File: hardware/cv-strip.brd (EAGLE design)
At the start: 152.5 x 43.6 mm, 83 parts, among them IC1 PIC16F1825SO14, IC2 74HC595D, IC3 74HC595D, IC4 MCP4728_QUAD_DAC, IC5 LM324D, IC6 REG1117, IC7 6N138

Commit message: add comp values
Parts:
- C18, C19, C9: value (none) -> 100n
- R17, R18, R19, R20, R23, R24, R25, R26: value (none) -> 100k
- R21, R22: value (none) -> 4k7
- R27, R28: value (none) -> 1k5
- R4: value (none) -> 10k
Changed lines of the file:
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@@
 <attribute name="VALUE" x="55.118" y="12.319" size="1.27" layer="28" rot="MR90"/>
 </element>
-<element name="R22" library="rcl" package="R0805" value="" x="63.5" y="33.02" smashed="yes" rot="MR270">
+<element name="R22" library="rcl" package="R0805" value="4k7" x="63.5" y="33.02" smashed="yes" rot="MR270">
 <attribute name="NAME" x="61.214" y="30.988" size="1.27" layer="26" rot="MR90"/>
-<attribute name="VALUE" x="66.04" y="33.655" size="1.27" layer="28" rot="MR270"/>
-</element>
-<element name="R21" library="rcl" package="R0805" value="" x="66.04" y="33.02" smashed="yes" rot="MR270">
+</element>
+<element name="R21" library="rcl" package="R0805" value="4k7" x="66.04" y="33.02" smashed="yes" rot="MR270">
 <attribute name="NAME" x="68.58" y="34.417" size="1.27" layer="26" rot="MR270"/>
-<attribute name="VALUE" x="68.58" y="33.655" size="1.27" layer="28" rot="MR270"/>
 </element>
 <element name="IC5" library="linear" package="SO14" value="LM324D" x="50.165" y="36.83" smashed="yes" rot="MR270">
 <attribute name="NAME" x="53.848" y="35.306" size="1.27" layer="26" rot="MR90"/>
 </element>
-<element name="R17" library="rcl" package="R0805" value="" x="57.15" y="40.64" smashed="yes" rot="MR0">
+<element name="R17" library="rcl" package="R0805" value="100k" x="57.15" y="40.64" smashed="yes" rot="MR0">
 <attribute name="NAME" x="62.611" y="40.132" size="1.27" layer="26" rot="MR0"/>
-<attribute name="VALUE" x="57.785" y="38.1" size="1.27" layer="28" rot="MR0"/>
-</element>
-<element name="R20" library="rcl" package="R0805" value="" x="57.023" y="33.02" smashed="yes" rot="MR0">
+</element>
+<element name="R20" library="rcl" package="R0805" value="100k" x="57.023" y="33.02" smashed="yes" rot="MR0">
 <attribute name="NAME" x="60.325" y="30.607" size="1.27" layer="26" rot="MR0"/>
-<attribute name="VALUE" x="57.658" y="30.48" size="1.27" layer="28" rot="MR0"/>
-</element>
-<element name="R26" library="rcl" package="R0805" value="" x="43.18" y="33.02" smashed="yes" rot="MR180">
+</element>
+<element name="R26" library="rcl" package="R0805" value="100k" x="43.18" y="33.02" smashed="yes" rot="MR180">
 <attribute name="NAME" x="37.846" y="33.655" size="1.27" layer="26" rot="MR180"/>
-<attribute name="VALUE" x="42.545" y="35.56" size="1.27" layer="28" rot="MR180"/>
-</element>
-<element name="R23" library="rcl" package="R0805" value="" x="43.18" y="40.64" smashed="yes" rot="MR180">
+</element>
+<element name="R23" library="rcl" package="R0805" value="100k" x="43.18" y="40.64" smashed="yes" rot="MR180">
 <attribute name="NAME" x="37.846" y="38.735" size="1.27" layer="26" rot="MR180"/>
-<attribute name="VALUE" x="42.545" y="43.18" size="1.27" layer="28" rot="MR180"/>
-</element>
-<element name="R18" library="rcl" package="R0805" value="" x="57.15" y="38.354" smashed="yes" rot="MR0">
+</element>
+<element name="R18" library="rcl" package="R0805" value="100k" x="57.15" y="38.354" smashed="yes" rot="MR0">
 <attribute name="NAME" x="62.611" y="38.227" size="1.27" layer="26" rot="MR0"/>
-<attribute name="VALUE" x="57.785" y="35.814" size="1.27" layer="28" rot="MR0"/>
-</element>
-<element name="R19" library="rcl" package="R0805" value="" x="57.023" y="35.306" smashed="yes" rot="MR0">
+</element>
+<element name="R19" library="rcl" package="R0805" value="100k" x="57.023" y="35.306" smashed="yes" rot="MR0">
 <attribute name="NAME" x="62.357" y="34.417" size="1.27" layer="26" rot="MR0"/>
-<attribute name="VALUE" x="57.658" y="32.766" size="1.27" layer="28" rot="MR0"/>
-</element>
-<element name="R25" library="rcl" package="R0805" value="" x="43.18" y="35.56" smashed="yes" rot="MR0">
+</element>
+<element name="R25" library="rcl" package="R0805" value="100k" x="43.18" y="35.56" smashed="yes" rot="MR0">
 <attribute name="NAME" x="41.148" y="34.925" size="1.27" layer="26" rot="MR0"/>
-<attribute name="VALUE" x="43.815" y="33.02" size="1.27" layer="28" rot="MR0"/>
-</element>
-<element name="R24" library="rcl" package="R0805" value="" x="43.18" y="38.1" smashed="yes" rot="MR0">
+</element>
+<element name="R24" library="rcl" package="R0805" value="100k" x="43.18" y="38.1" smashed="yes" rot="MR0">
 <attribute name="NAME" x="41.021" y="40.005" size="1.27" layer="26" rot="MR0"/>
-<attribute name="VALUE" x="43.815" y="35.56" size="1.27" layer="28" rot="MR0"/>
 </element>
 <element name="C13" library="rcl" package="C0805" value="" x="89.662" y="1.143" smashed="yes" rot="MR180">
@@
 <attribute name="VALUE" x="88.392" y="3.683" size="1.27" layer="28" rot="MR180"/>
 </element>
-<element name="C9" library="rcl" package="C0805" value="" x="87.122" y="29.718" smashed="yes" rot="MR0">
+<element name="C9" library="rcl" package="C0805" value="100n" x="87.122" y="29.718" smashed="yes" rot="MR0">
 <attribute name="NAME" x="88.773" y="27.178" size="1.27" layer="26" rot="MR0"/>
-<attribute name="VALUE" x="88.392" y="27.178" size="1.27" layer="28" rot="MR0"/>
-</element>
-<element name="C19" library="rcl" package="C0805" value="" x="57.023" y="29.464" smashed="yes" rot="MR0">
+</element>
+<element name="C19" library="rcl" package="C0805" value="100n" x="57.023" y="29.464" smashed="yes" rot="MR0">
 <attribute name="NAME" x="56.388" y="27.051" size="1.27" layer="26" rot="MR0"/>
-<attribute name="VALUE" x="58.293" y="26.924" size="1.27" layer="28" rot="MR0"/>
 </element>
 <element name="C17" library="rcl" package="C0805" value="" x="66.675" y="13.081" smashed="yes" rot="MR270">
@@
 <attribute name="NAME" x="22.903" y="32.0118" size="1" layer="22" rot="MR270"/>
 </element>
-<element name="R27" library="rcl" package="R0805" value="" x="31.75" y="36.83" smashed="yes" rot="MR90">
+<element name="R27" library="rcl" package="R0805" value="1k5" x="31.75" y="36.83" smashed="yes" rot="MR90">
 <attribute name="NAME" x="29.083" y="35.306" size="1.27" layer="26" rot="MR90"/>
-<attribute name="VALUE" x="29.21" y="36.195" size="1.27" layer="28" rot="MR90"/>
-</element>
-<element name="R28" library="rcl" package="R0805" value="" x="30.48" y="31.75" smashed="yes" rot="MR270">
+</element>
+<element name="R28" library="rcl" package="R0805" value="1k5" x="30.48" y="31.75" smashed="yes" rot="MR270">
 <attribute name="NAME" x="33.147" y="32.004" size="1.27" layer="26" rot="MR270"/>
-<attribute name="VALUE" x="33.02" y="32.385" size="1.27" layer="28" rot="MR270"/>
 </element>
 <element name="DRM1" library="jason_eagle6" package="VERTICAL_3_5MM_SOCKET" value="VERTICAL_3_5MM_SOCKET" x="106.68" y="21.59" smashed="yes">
@@
 <attribute name="VALUE" x="110.998" y="40.64" size="1.27" layer="27" ratio="10" rot="R180"/>
 </element>
-<element name="R4" library="rcl" package="R0805" value="" x="100.33" y="35.56" smashed="yes" rot="MR270">
+<element name="R4" library="rcl" package="R0805" value="10k" x="100.33" y="35.56" smashed="yes" rot="MR270">
 <attribute name="NAME" x="101.6" y="36.068" size="1.27" layer="26" rot="MR180"/>
-<attribute name="VALUE" x="102.87" y="36.195" size="1.27" layer="28" rot="MR270"/>
-</element>
-<element name="C18" library="rcl" package="C0805" value="" x="62.23" y="36.83" smashed="yes" rot="MR180">
+</element>
+<element name="C18" library="rcl" package="C0805" value="100n" x="62.23" y="36.83" smashed="yes" rot="MR180">
 <attribute name="NAME" x="64.643" y="37.465" size="1.27" layer="26" rot="MR180"/>
-<attribute name="VALUE" x="60.96" y="39.37" size="1.27" layer="28" rot="MR180"/>
 </element>
 <element name="U$2" library="jason_eagle6" package="PWR_SOCKET_2_1MM" value="PWR_SOCKET_2_1MM" x="138.905" y="35.687" smashed="yes" rot="R45"/>

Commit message: rev2 updates - checking needed
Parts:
- removed CLK1, CLK2, DRM1, DRM2, DRM3, DRM4, DRM5, DRM6, DRM7, DRM8, GATE1, GATE2, NOTE1CV, NOTE2CV, VEL1CV, VEL2CV: VERTICAL_3_5MM_SOCKET, jason_eagle6:VERTICAL_3_5MM_SOCKET
- removed D2: 1N4004, jasons_stuff:DO-VERT
- removed L1, L2, L3: (no value), led:LED3MM
- removed S1: (no value), switch-omron:B3F-10XX
- added ACT, PWR, STA: (no value), led:LED3MM
- added C22: (no value), microbuilder:EIA3216-18/A-R
- added CVA, CVB, CVC, CVD, GT1, GT10, GT11, GT12, GT2, GT3, GT4, GT5, GT6, GT7, GT8, GT9: VERTICAL_3_5MM_SOCKET, jason_eagle6:VERTICAL_3_5MM_SOCKET
- added D3, D4, D5: (no value), microbuilder:SOD-123
- added MODE: (no value), switch-omron:B3F-10XX
- added Q1, Q2, Q4: (no value), microbuilder:SOT363
- added Q3, Q5: (no value), microbuilder:SOT23-R
- added R30, R31, R32, R33, R34, R35, R36, R37, R38, R39: (no value), rcl:R0805
- IC2: value 74HC595D -> AD5696R; device 74xx-eu:SO16 -> jason_eagle6:SSOP16
- IC3: value 74HC595D -> MC14094B; device 74xx-eu:SO16 -> jason_eagle6:SO16
- IC4: value MCP4728_QUAD_DAC -> MC14094B; device jason_eagle6:MSOP10 -> jason_eagle6:SO16
- moved IC4 55.4 mm to (100.6, 7.49)
- moved IC2 47.1 mm to (57.1, 32.3)
- moved R8 15.3 mm to (108.0, 11.4), turned to 180 degrees
- moved R10 14.0 mm to (128.9, 26.9), turned to 270 degrees
- moved R12 13.9 mm to (103.6, 26.7)
- moved R11 13.8 mm to (116.2, 26.5), turned to 270 degrees
- moved C7 11.7 mm to (120.7, 24.1), turned to 180 degrees
- moved C8 11.7 mm to (108.0, 24.1), turned to 180 degrees
- moved C6 11.6 mm to (133.3, 24.1), turned to 180 degrees
- moved R6 11.6 mm to (129.4, 14.2)
- moved R7 11.5 mm to (116.2, 14.2)
- moved C13 11.4 mm to (83.8, 10.9), turned to 270 degrees
- moved C4 9.72 mm to (112.3, 16.0), turned to 90 degrees
- moved C3 9.59 mm to (125.0, 16.1), turned to 90 degrees
- moved C2 9.55 mm to (137.2, 16.1), turned to 90 degrees
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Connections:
- removed net MIDI_OUT: IC1.6
- removed net N$22: IC1.9, IC4.3, R21.2
- removed net N$47: IC2.3, R5.1
- removed net N$51: IC2.4, R12.1
- removed net N$53: IC2.7, R9.1
- new net GT1_VSEL: IC1.6, R38.1
- new net GT2_VSEL: IC1.7, R39.1
- new net N$10: IC3.5, R15.1
- new net N$11: IC3.7, R16.1
- new net N$14: IC3.1, Q1.3, R31.1
- new net N$17: IC4.11, R9.1
- new net N$18: IC4.12, R10.1
- new net N$19: IC4.13, R11.1
- new net N$38: IC4.14, R12.1
- new net N$44: IC4.6, R6.1
- new net N$45: IC4.5, R7.1
- new net SCL: IC1.10, IC2.P$13, R22.2
- new net SDA: IC1.9, IC2.P$8, R21.2
- new net VDD_GT1: C13.1, D3.C, IC3.15, IC3.16, Q3.3, R30.2, R31.2, R32.2
- new net VDD_GT2: C12.1, D4.C, IC4.15, IC4.16, Q5.3, R33.2, R34.2, R35.2
- net ACT_LED: now also ACT.A; no longer L1.A
- net GND: now also C22.-, C9.2, CVA.2, CVB.2, CVC.2, CVD.2, GT1.2, GT10.2, GT11.2, GT12.2, GT2.2, GT3.2, GT4.2, GT5.2, GT6.2, GT7.2, GT8.2, GT9.2, IC2.P$12, IC2.P$14, IC2.P$16, IC2.P$4, IC2.P$9, IC4.8, MODE.3, MODE.4, Q1.1, Q1.4, Q2.1, Q2.4, Q4.1, Q4.4; no longer C9.1, CLK1.2, CLK2.2, DRM1.2, DRM2.2, DRM3.2, DRM4.2, DRM5.2, DRM6.2, DRM7.2, DRM8.2, GATE1.2, GATE2.2, IC2.13, IC2.8, IC3.13, IC4.10, IC4.4, NOTE1CV.2, NOTE2CV.2, S1.3, S1.4, VEL1CV.2, VEL2CV.2
- net N$1: now also GT4.4; no longer CLK2.4
- net N$12: now also IC3.6, R14.1; no longer IC3.15, R15.1
- net N$13: now also IC3.4, R13.1; no longer IC3.1, R16.1
- net N$15: now also IC3.2, Q1.6, R30.1; no longer IC3.3, R13.1
- net N$16: now also IC3.3, Q2.6, R32.1; no longer IC3.2, R14.1
- net N$2: now also CVD.4; no longer VEL2CV.4
- net N$20: now also GT9.4; no longer DRM1.4
- net N$21: now also Q5.1, R37.1, R39.2; no longer IC1.10, IC4.2, R22.2
- net N$23: now also GT10.4; no longer DRM2.4
- net N$24: now also GT11.4; no longer DRM3.4
- net N$3: now also CVB.4; no longer VEL1CV.4
- net N$32: now also GT8.4; no longer DRM4.4
- net N$33: now also GT5.4; no longer DRM5.4
- net N$34: now also MODE.1, MODE.2, R4.2
- net N$35: now also PWR.K; no longer L3.K
- net N$36: now also ACT.K; no longer L1.K
- net N$37: now also STA.K; no longer L2.K
- net N$39: now also GT6.4; no longer DRM6.4
- net N$4: now also CVC.4; no longer NOTE1CV.4
- net N$40: now also D5.A; no longer D2.A
- net N$41: now also GT7.4; no longer DRM7.4
- net N$43: now also IC4.7, R5.1; no longer IC2.15, R8.1
- net N$46: now also IC4.4, R8.1; no longer IC2.1, R7.1
- net N$48: now also IC4.1, Q2.3, R33.1; no longer IC2.2, R6.1
- net N$49: now also IC4.2, Q4.3, R34.1; no longer IC2.5, R11.1
- net N$5: now also CVA.4; no longer NOTE2CV.4
- net N$50: now also IC4.3, Q4.6, R35.1; no longer IC2.6, R10.1
- net N$52: now also GT12.4; no longer DRM8.4
- net N$6: now also GT3.4; no longer GATE2.4
- net N$7: now also GT1.4; no longer GATE1.4
- net N$8: now also GT2.4; no longer CLK1.4
- net N$9: now also Q3.1, R36.1, R38.2; no longer IC1.7, R4.2, S1.1, S1.2
- net SR_CLK: now also Q2.5, Q4.5; no longer IC2.11, IC3.11
- net SR_DAT: now also Q1.5; no longer IC3.14
- net SR_DAT2: now also Q4.2; no longer IC2.14
- net SR_RCK: now also Q1.2, Q2.2; no longer IC2.12, IC3.12
- net STATUS_LED: now also STA.A; no longer L2.A
- net VDD: now also C22.+, C9.1, D3.A, D4.A, IC2.P$10, IC2.P$11, IC2.P$15, IC2.P$5, PWR.A; no longer C12.1, C13.1, C9.2, IC2.10, IC2.16, IC3.10, IC3.16, IC4.1, L3.A
- net VIN: now also D5.C, Q3.2, Q5.2, R36.2, R37.2; no longer D2.C
- net VOUTA: now also IC2.P$3, IC5.3; no longer IC4.6, IC5.5
- net VOUTB: now also IC2.P$2, IC5.5; no longer IC4.7, IC5.3
- net VOUTC: now also IC2.P$6; no longer IC4.8
- net VOUTD: now also IC2.P$7; no longer IC4.9
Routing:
- net VIN: track 51.3 -> 169.3 mm, vias 2 -> 3
- net VDD_GT1: track 0.00 -> 88.5 mm, vias 0 -> 2
- net VDD_GT2: track 0.00 -> 76.0 mm, vias 0 -> 4
- net N$47: track 73.4 -> 0.00 mm, vias 2 -> 0
- net GT2_VSEL: track 0.00 -> 72.1 mm, vias 0 -> 2
- net GT1_VSEL: track 0.00 -> 62.2 mm, vias 0 -> 2
- net SCL: track 0.00 -> 55.3 mm, vias 0 -> 3
- net N$53: track 53.7 -> 0.00 mm
- net N$22: track 50.9 -> 0.00 mm, vias 3 -> 0
- net N$17: track 0.00 -> 50.5 mm, vias 0 -> 2
- net SDA: track 0.00 -> 48.1 mm, vias 0 -> 3
- net N$21: track 49.4 -> 4.79 mm, vias 3 -> 0
- net N$48: track 59.7 -> 17.1 mm
- net N$18: track 0.00 -> 41.9 mm, vias 0 -> 2
- net N$46: track 46.1 -> 6.67 mm, vias 2 -> 0
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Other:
- board text added: "POWER"
- board text added: "rev 2"
- board text removed: "rev 1"

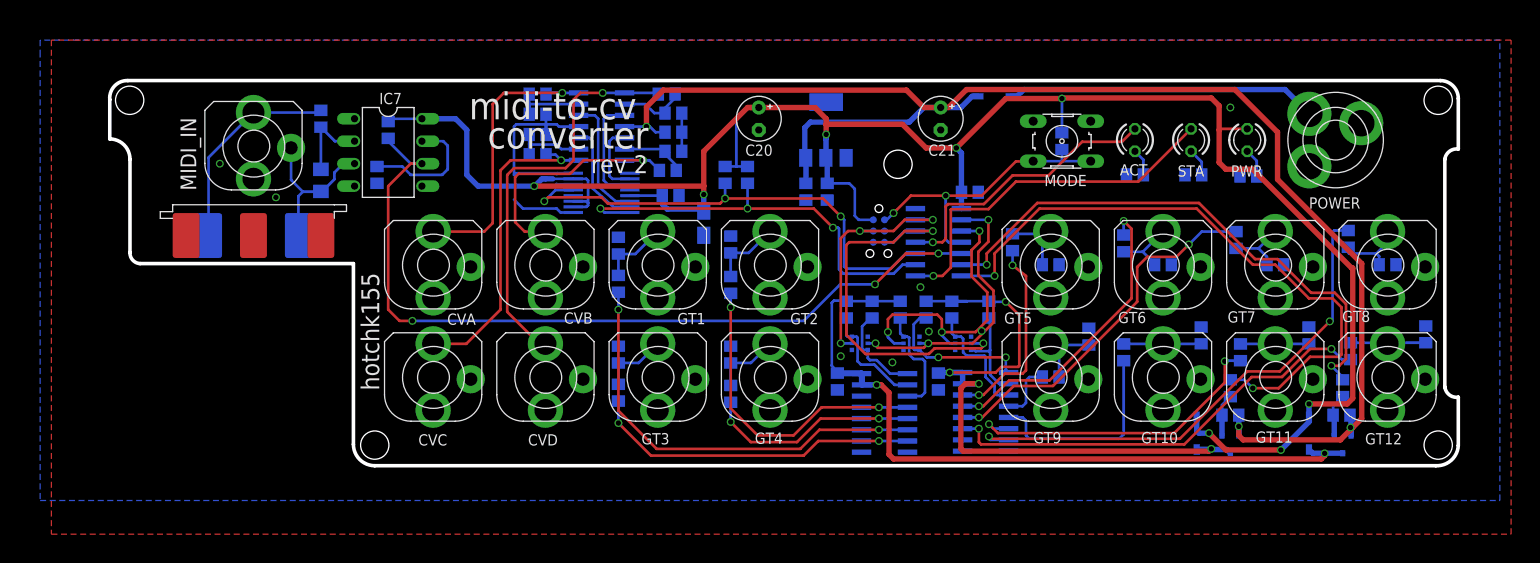
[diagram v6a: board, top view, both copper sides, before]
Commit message: extra n fet on voltage select circuits
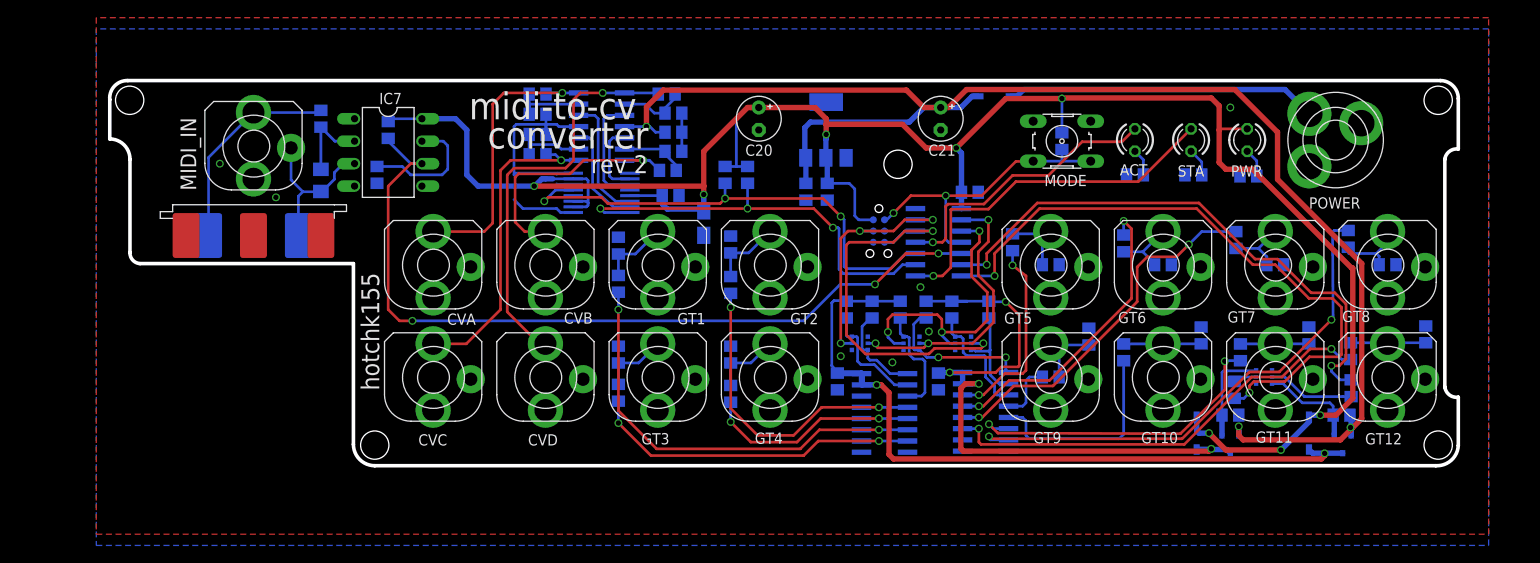
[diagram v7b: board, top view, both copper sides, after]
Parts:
- added Q8: (no value), microbuilder:SOT363
- moved R38 0.95 mm to (141.9, 10.2)
- moved R39 0.48 mm to (128.7, 9.97), turned to 90 degrees
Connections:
- new net N$22: Q8.2, R38.2
- new net N$47: Q8.5, R39.2
- net GND: now also Q8.1, Q8.4
- net N$21: now also Q8.6; no longer R39.2
- net N$9: now also Q8.3; no longer R38.2
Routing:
- net N$22: track 0.00 -> 9.86 mm
- net N$9: track 4.90 -> 11.3 mm
- net N$21: track 4.79 -> 11.1 mm
- net N$47: track 0.00 -> 3.69 mm
- net VIN: track 169.3 -> 168.0 mm
- net GT1_VSEL: track 62.2 -> 63.3 mm
- net VDD: track 244.0 -> 243.1 mm
- net GT2_VSEL: track 72.1 -> 72.9 mm
- net GND: vias 8 -> 7

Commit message: PCBrev2
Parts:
- added Q10, Q12, Q14: (no value), transistor:SOT23-BEC
- added Q11, Q13, Q7, Q9: (no value), microbuilder:SOT23-R
- added Q6: (no value), microbuilder:SOT363
- added R40, R41, R42, R43, R44, R45, R46, R47: (no value), rcl:R0805
- C10, C14, C15: value (none) -> 100n
- C16: device rcl:C0805 -> microbuilder:EIA3216-18/A-R
- C18, C19, C9: value 100n -> (none)
- C20: device resistor:E2,5-5 -> rcl:C0805
- C22: device microbuilder:EIA3216-18/A-R -> resistor:E2,5-5
- Q1, Q2: device microbuilder:SOT363 -> microbuilder:SOT23-R
- Q3, Q5: device microbuilder:SOT23-R -> microbuilder:SOT363
- Q8: device microbuilder:SOT363 -> transistor:SOT23-BEC
- moved Q8 61.3 mm to (72.5, 25.5), turned to 90 degrees
- moved Q1 55.8 mm to (141.0, 3.81), turned to 180 degrees
- moved Q2 37.8 mm to (128.3, 3.81), turned to 180 degrees
- moved Q5 37.8 mm to (92.2, 15.2), turned to 270 degrees
- moved C20 29.3 mm to (59.4, 15.8), flipped to the bottom, turned to 0 degrees
- moved C22 29.3 mm to (95.5, 40.6), flipped to the top, turned to 270 degrees
- moved C17 25.7 mm to (80.2, 28.5), turned to 180 degrees
- moved C21 20.6 mm to (74.9, 40.6)
- moved C11 18.5 mm to (80.3, 32.4), turned to 90 degrees
- moved C19 17.5 mm to (72.3, 16.0)
- moved C9 16.1 mm to (98.8, 32.3), turned to 0 degrees
- moved C16 15.0 mm to (69.1, 28.7)
- moved C14 14.3 mm to (65.3, 39.1), turned to 180 degrees
- moved R15 13.5 mm to (58.7, 6.22), turned to 270 degrees
- moved R13 13.1 mm to (58.6, 21.6), turned to 270 degrees
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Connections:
- new net GT1: C18.1, GT1.4, R40.1, R47.2
- new net GT1H: IC3.7, Q9.1
- new net GT1L: IC3.11, R13.2
- new net GT2: C17.1, GT2.4, R41.1, R44.2
- new net GT2H: IC3.4, Q7.1
- new net GT2L: IC3.14, R14.2
- new net GT3: C20.1, GT3.4, R42.1, R45.2
- new net GT3H: IC3.6, Q13.1
- new net GT3L: IC3.12, R15.2
- new net GT4: C19.1, GT4.4, R43.1, R46.2
- new net GT4H: IC3.5, Q11.1
- new net GT4L: IC3.13, R16.2
- new net N$51: Q14.C, R45.1
- new net N$53: Q9.3, R40.2
- new net N$54: Q12.C, R46.1
- new net N$55: Q10.C, R47.1
- net GND: now also C10.2, C15.1, C16.-, C19.2, C20.2, C9.1, Q10.E, Q12.E, Q14.E, Q3.1, Q3.4, Q5.1, Q5.4, Q6.1, Q6.4, Q8.E; no longer C10.1, C15.2, C16.2, C19.1, C20.-, C9.2, Q1.1, Q1.4, Q2.1, Q2.4, Q8.1, Q8.4
- net N$1: now also Q7.3, R41.2; no longer C16.1, GT4.4, R15.2
- net N$10: now also Q8.B, R14.1; no longer IC3.5, R15.1
- net N$11: now also Q14.B, R15.1; no longer IC3.7, R16.1
- net N$12: now also Q12.B, R16.1; no longer IC3.6, R14.1
- net N$13: now also Q8.C, R44.1; no longer IC3.4, R13.1
- net N$14: now also Q6.3; no longer Q1.3
- net N$15: now also Q6.6; no longer Q1.6
- net N$16: now also Q5.6; no longer Q2.6
- net N$20: now also C8.1; no longer C4.1
- net N$21: now also Q2.1, Q3.6; no longer Q5.1, Q8.6
- net N$22: now also Q3.2; no longer Q8.2
- net N$23: now also C7.1; no longer C3.1
- net N$24: now also C6.1; no longer C2.1
- net N$33: now also C4.1; no longer C8.1
- net N$39: now also C3.1; no longer C7.1
- net N$41: now also C2.1; no longer C6.1
- net N$47: now also Q3.5; no longer Q8.5
- net N$48: now also Q5.3; no longer Q2.3
- net N$6: now also Q13.3, R42.2; no longer C17.1, GT3.4, R16.2
- net N$7: now also Q11.3, R43.2; no longer C15.1, GT1.4, R14.2
- net N$8: now also Q10.B, R13.1; no longer C14.1, GT2.4, R13.2
- net N$9: now also Q1.1, Q3.3; no longer Q3.1, Q8.3
- net SR_CLK: now also Q5.5; no longer Q2.5
- net SR_DAT: now also Q6.5; no longer Q1.5
- net SR_RCK: now also Q5.2, Q6.2; no longer Q1.2, Q2.2
- net VDD: now also C10.1, C15.2, C16.+, C21.+, C9.2; no longer C11.2, C19.2, C20.+, C22.+, C9.1
- net VDD_GT1: now also Q1.3, Q11.2, Q13.2, Q7.2, Q9.2; no longer Q3.3
- net VDD_GT2: now also Q2.3; no longer Q5.3
- net VIN: now also C11.2, C14.1, C22.+, Q1.2, Q2.2; no longer C10.2, C18.1, C21.+, Q3.2, Q5.2
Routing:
- net GT1H: track 0.00 -> 60.8 mm, vias 0 -> 2
- net GT1L: track 0.00 -> 47.1 mm, vias 0 -> 2
- net N$12: track 48.8 -> 1.94 mm, vias 2 -> 0
- net GT3H: track 0.00 -> 37.4 mm, vias 0 -> 2
- net N$11: track 37.4 -> 1.85 mm, vias 2 -> 0
- net N$13: track 35.6 -> 3.94 mm, vias 2 -> 0
- net VDD_GT1: track 88.5 -> 119.6 mm, vias 2 -> 6
- net GT3L: track 0.00 -> 30.6 mm
- net GT2L: track 0.00 -> 28.1 mm, vias 0 -> 2
- net N$10: track 24.3 -> 2.05 mm, vias 2 -> 0
- net GT2H: track 0.00 -> 21.6 mm, vias 0 -> 2
- net GT4L: track 0.00 -> 18.0 mm
- net GT4H: track 0.00 -> 15.5 mm, vias 0 -> 2
- net GT1: track 0.00 -> 11.3 mm
- net GT2: track 0.00 -> 10.9 mm
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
